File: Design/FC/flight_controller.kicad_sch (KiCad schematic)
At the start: 44 parts, among them U1 STM32H747BIT6, U3 BMI323, U4 MMC5983MA, U5 BMP390

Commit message: before shrinking pcb
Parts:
- removed R64: 0, symbol Device:R_Small_US
- added NT7, NT8: NT, Lib:NetTie-2_SMD_Track0.35mm, symbol Device:NetTie_2
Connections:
- net +3.3V: now also NT7.1
- net BARO_INT_1: now also U1.34 (PF10); no longer U1.26 (PF4)
- net BARO_SPI_NSS: now also U1.30 (PF6); no longer U1.25 (PF3)
- net GND: now also NT8.2; no longer U1.194 (BOOT0)
- net MAG_SPI_NSS: now also U1.26 (PF4); no longer U1.34 (PF10)
- net NRST: now also NT7.2
- net R_SERVO_2_SIGNAL: no longer U1.205 (PI6)
- net EXT_6_DEV_INT_MAG renamed EXT_3_DEV_INT
- net EXT_3_DEV_INT: now also U1.25 (PF3); no longer U1.30 (PF6)
- new net BOOT0: NT8.1, U1.194 (BOOT0)
- no-connect marks 106 -> 107
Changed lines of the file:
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@@
 	)
 	(no_connect
+		(at 57.15 392.43)
+	)
+	(no_connect
 		(at 55.88 248.92)
 	)
@@
 	(wire
 		(pts
-			(xy 52.07 392.43) (xy 57.15 392.43)
-		)
-		(stroke
-			(width 0)
-			(type default)
-		)
-	)
-	(wire
-		(pts
 			(xy 91.44 82.55) (xy 100.33 82.55)
 		)
@@
 	(wire
 		(pts
-			(xy 102.87 382.27) (xy 110.49 382.27)
+			(xy 102.87 382.27) (xy 114.3 382.27)
 		)
 		(stroke
@@
 		)
 	)
+	(label "BOOT0"
+		(at 104.14 382.27 0)
+		(effects
+			(font
+				(size 1.27 1.27)
+			)
+			(justify left bottom)
+		)
+	)
 	(global_label "LED_FC_4"
 		(shape input)
@@
 		)
 	)
-	(global_label "EXT_3_DEV_INT_BARO"
+	(global_label "EXT_10_DEV_INT"
 		(shape input)
-		(at 55.88 297.18 180)
+		(at 55.88 314.96 180)
 		(fields_autoplaced yes)
 		(effects
@@
 		)
 		(property "Intersheetrefs" "${INTERSHEET_REFS}"
-			(at 33.1192 297.18 0)
+			(at 37.8364 314.96 0)
 			(effects
 				(font
@@
 		)
 	)
-	(global_label "SPI_5_NSS_MAG"
+	(global_label "SPI_5_NSS_1"
 		(shape input)
 		(at 91.44 60.96 180)
@@
 		)
 		(property "Intersheetrefs" "${INTERSHEET_REFS}"
-			(at 73.6987 60.96 0)
+			(at 76.2992 60.96 0)
 			(effects
 				(font
@@
 		)
 	)
-	(global_label "EXT_6_DEV_INT_MAG"
+	(global_label "EXT_3_DEV_INT"
 		(shape input)
 		(at 91.44 63.5 180)
@@
 		)
 		(property "Intersheetrefs" "${INTERSHEET_REFS}"
-			(at 69.8283 63.5 0)
+			(at 74.6059 63.5 0)
 			(effects
 				(font
@@
 		)
 	)
-	(global_label "EXT_6_DEV_INT_MAG"
+	(global_label "EXT_3_DEV_INT"
 		(shape input)
-		(at 55.88 304.8 180)
+		(at 55.88 297.18 180)
 		(fields_autoplaced yes)
 		(effects
@@
 		)
 		(property "Intersheetrefs" "${INTERSHEET_REFS}"
-			(at 34.2683 304.8 0)
+			(at 39.0459 297.18 0)
 			(effects
 				(font
@@
 		)
 	)
-	(global_label "EXT_3_DEV_INT_BARO"
+	(global_label "EXT_10_DEV_INT"
 		(shape input)
-		(at 91.44 80.01 180)
+		(at 91.44 82.55 180)
 		(fields_autoplaced yes)
 		(effects
@@
 		)
 		(property "Intersheetrefs" "${INTERSHEET_REFS}"
-			(at 68.6792 80.01 0)
+			(at 73.3964 82.55 0)
 			(effects
 				(font
@@
 		)
 	)
-	(global_label "SPI_5_NSS_MAG"
+	(global_label "SPI_5_NSS_1"
 		(shape input)
-		(at 55.88 314.96 180)
+		(at 55.88 299.72 180)
 		(fields_autoplaced yes)
 		(effects
@@
 		)
 		(property "Intersheetrefs" "${INTERSHEET_REFS}"
-			(at 38.1387 314.96 0)
+			(at 40.7392 299.72 0)
 			(effects
 				(font
@@
 		)
 	)
-	(global_label "TIM_8_CH_2"
-		(shape input)
-		(at 52.07 392.43 180)
-		(fields_autoplaced yes)
-		(effects
-			(font
-				(size 1.27 1.27)
-			)
-			(justify right)
-		)
-		(property "Intersheetrefs" "${INTERSHEET_REFS}"
-			(at 38.1387 392.43 0)
-			(effects
-				(font
-					(size 1.27 1.27)
-				)
-				(justify right)
-				(hide yes)
-			)
-		)
-	)
 	(global_label "BARO_SPI_MISO"
 		(shape input)
@@
 		)
 	)
-	(global_label "SPI_5_NSS_BARO"
+	(global_label "SPI_5_NSS_2"
 		(shape input)
-		(at 91.44 82.55 180)
+		(at 91.44 80.01 180)
 		(fields_autoplaced yes)
 		(effects
@@
 		)
 		(property "Intersheetrefs" "${INTERSHEET_REFS}"
-			(at 72.5496 82.55 0)
+			(at 76.2992 80.01 0)
 			(effects
 				(font
@@
 		)
 	)
-	(global_label "SPI_5_NSS_BARO"
+	(global_label "SPI_5_NSS_2"
 		(shape input)
-		(at 55.88 299.72 180)
+		(at 55.88 304.8 180)
 		(fields_autoplaced yes)
 		(effects
@@
 		)
 		(property "Intersheetrefs" "${INTERSHEET_REFS}"
-			(at 36.9896 299.72 0)
+			(at 40.7392 304.8 0)
 			(effects
 				(font
@@
 	)
 	(symbol
+		(lib_id "Device:NetTie_2")
+		(at 116.84 382.27 0)
+		(unit 1)
+		(exclude_from_sim no)
+		(in_bom no)
+		(on_board yes)
+		(dnp no)
+		(property "Reference" "NT8"
+			(at 116.84 381 0)
+			(effects
+				(font
+					(size 1.27 1.27)
+				)
+			)
+		)
+		(property "Value" "NT"
+			(at 117.094 383.54 0)
+			(effects
+				(font
+					(size 1.27 1.27)
+				)
+			)
+		)
+		(property "Footprint" "Lib:NetTie-2_SMD_Track0.35mm"
+			(at 116.84 382.27 0)
+			(effects
+				(font
+					(size 1.27 1.27)
+				)
+				(hide yes)
+			)
+		)
+		(property "Datasheet" "~"
+			(at 116.84 382.27 0)
+			(effects
+				(font
+					(size 1.27 1.27)
+				)
+				(hide yes)
+			)
+		)
+		(property "Description" "Net tie, 2 pins"
+			(at 116.84 382.27 0)
+			(effects
+				(font
+					(size 1.27 1.27)
+				)
+				(hide yes)
+			)
+		)
+		(pin "1"
+		)
+		(pin "2"
+		)
+		(instances
+			(project "fc"
+				(path "/b150e79a-000e-446c-9119-0865a2de86ff/ef3444a3-41e3-41ea-8a4e-a671b048941e"
+					(reference "NT8")
+					(unit 1)
+				)
+			)
+		)
+	)
+	(symbol
 		(lib_id "Connector_Generic:Conn_01x03")
 		(at 195.58 184.15 90)
@@
 	(symbol
 		(lib_id "power:GND")
-		(at 110.49 382.27 0)
+		(at 119.38 382.27 0)
 		(unit 1)
 		(exclude_from_sim no)
@@
 		(dnp no)
 		(property "Reference" "#PWR086"
-			(at 110.49 388.62 0)
+			(at 119.38 388.62 0)
 			(effects
 				(font
@@
 		)
 		(property "Value" "GND"
-			(at 110.49 386.334 0)
+			(at 119.38 386.334 0)
 			(effects
 				(font
@@
 		)
 		(property "Footprint" ""
-			(at 110.49 382.27 0)
+			(at 119.38 382.27 0)
 			(effects
 				(font
@@
 		)
 		(property "Datasheet" ""
-			(at 110.49 382.27 0)
+			(at 119.38 382.27 0)
 			(effects
 				(font
@@
 		)
 		(property "Description" "Power symbol creates a global label with name \"GND\" , ground"
-			(at 110.49 382.27 0)
+			(at 119.38 382.27 0)
 			(effects
 				(font
@@
 	)
 	(symbol
+		(lib_id "Device:NetTie_2")
+		(at 180.34 52.07 270)
+		(unit 1)
+		(exclude_from_sim no)
+		(in_bom no)
+		(on_board yes)
+		(dnp no)
+		(fields_autoplaced yes)
+		(property "Reference" "NT7"
+			(at 181.61 50.7999 90)
+			(effects
+				(font
+					(size 1.27 1.27)
+				)
+				(justify left)
+			)
+		)
+		(property "Value" "NT"
+			(at 181.61 53.3399 90)
+			(effects
+				(font
+					(size 1.27 1.27)
+				)
+				(justify left)
+			)
+		)
+		(property "Footprint" "Lib:NetTie-2_SMD_Track0.35mm"
+			(at 180.34 52.07 0)
+			(effects
+				(font
+					(size 1.27 1.27)
+				)
+				(hide yes)
+			)
+		)
+		(property "Datasheet" "~"
+			(at 180.34 52.07 0)
+			(effects
+				(font
+					(size 1.27 1.27)
+				)
+				(hide yes)
+			)
+		)
+		(property "Description" "Net tie, 2 pins"
+			(at 180.34 52.07 0)
+			(effects
+				(font
+					(size 1.27 1.27)
+				)
+				(hide yes)
+			)
+		)
+		(pin "1"
+		)
+		(pin "2"
+		)
+		(instances
+			(project "fc"
+				(path "/b150e79a-000e-446c-9119-0865a2de86ff/ef3444a3-41e3-41ea-8a4e-a671b048941e"
+					(reference "NT7")
+					(unit 1)
+				)
+			)
+		)
+	)
+	(symbol
 		(lib_id "power:+5V")
 		(at 193.04 223.52 0)
@@
 					(unit 1)
 				)
-			)
-		)
-	)
-	(symbol
-		(lib_id "Device:R_Small_US")
-		(at 180.34 52.07 180)
-		(unit 1)
-		(exclude_from_sim no)
-		(in_bom no)
-		(on_board no)
-		(dnp no)
-		(property "Reference" "R64"
-			(at 179.324 53.34 0)
-			(effects
-				(font
-					(size 1.27 1.27)
-				)
-				(justify left)
-				(hide yes)
-			)
-		)
-		(property "Value" "0"
-			(at 179.324 51.816 0)
-			(effects
-				(font
-					(size 1.27 1.27)
-				)
-				(justify left)
-			)
-		)
-		(property "Footprint" ""
-			(at 180.34 52.07 0)
-			(effects
-				(font
-					(size 1.27 1.27)
-				)
-				(hide yes)
-			)
-		)
-		(property "Datasheet" "~"
-			(at 180.34 52.07 0)
-			(effects
-				(font
-					(size 1.27 1.27)
-				)
-				(hide yes)
-			)
-		)
-		(property "Description" "Resistor, small US symbol"
-			(at 180.34 52.07 0)
-			(effects
-				(font
-					(size 1.27 1.27)
-				)
-				(hide yes)
-			)
-		)
-		(pin "1"
-		)
-		(pin "2"
-		)
-		(instances
-			(project "fc"
-				(path "/b150e79a-000e-446c-9119-0865a2de86ff/ef3444a3-41e3-41ea-8a4e-a671b048941e"
-					(reference "R64")
-					(unit 1)
-				)

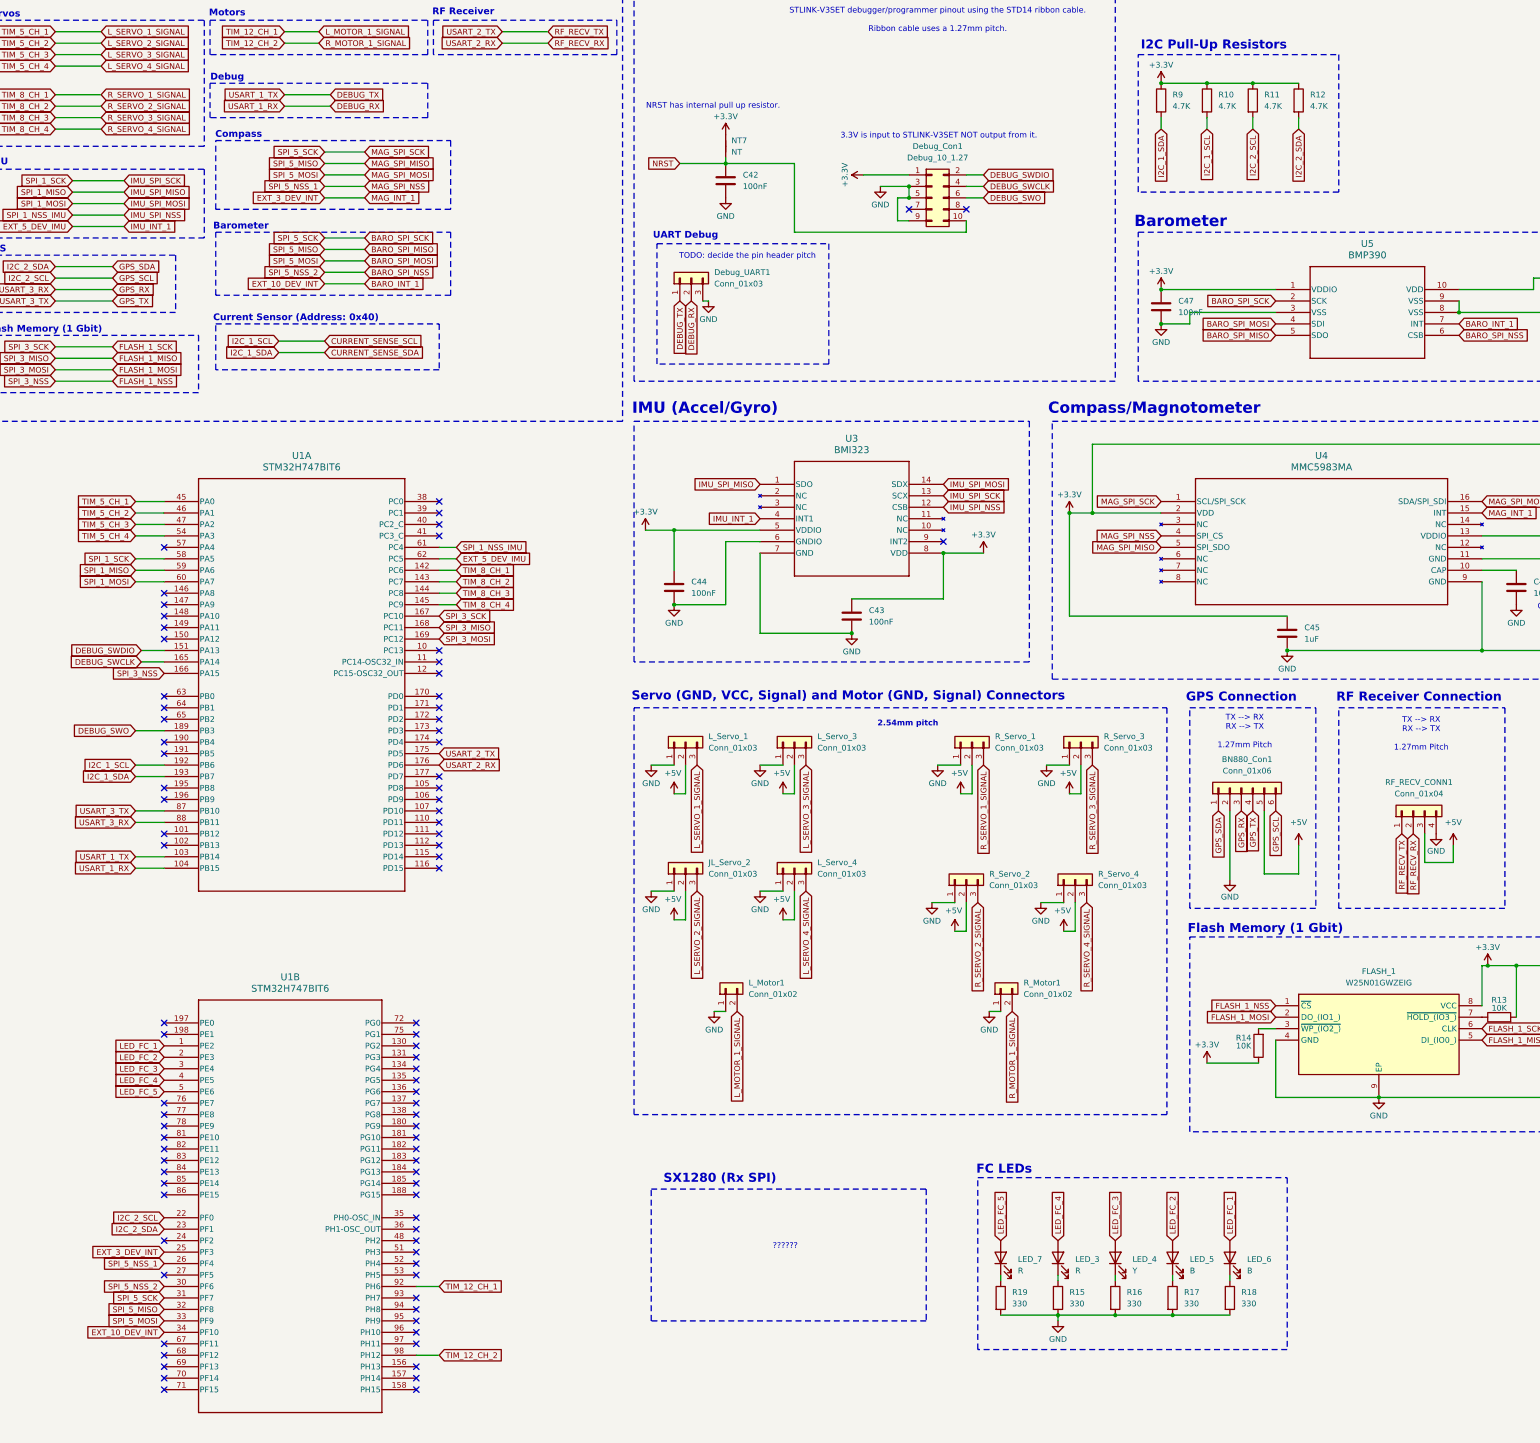
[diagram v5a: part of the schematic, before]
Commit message: finished pcb layout and started on bom
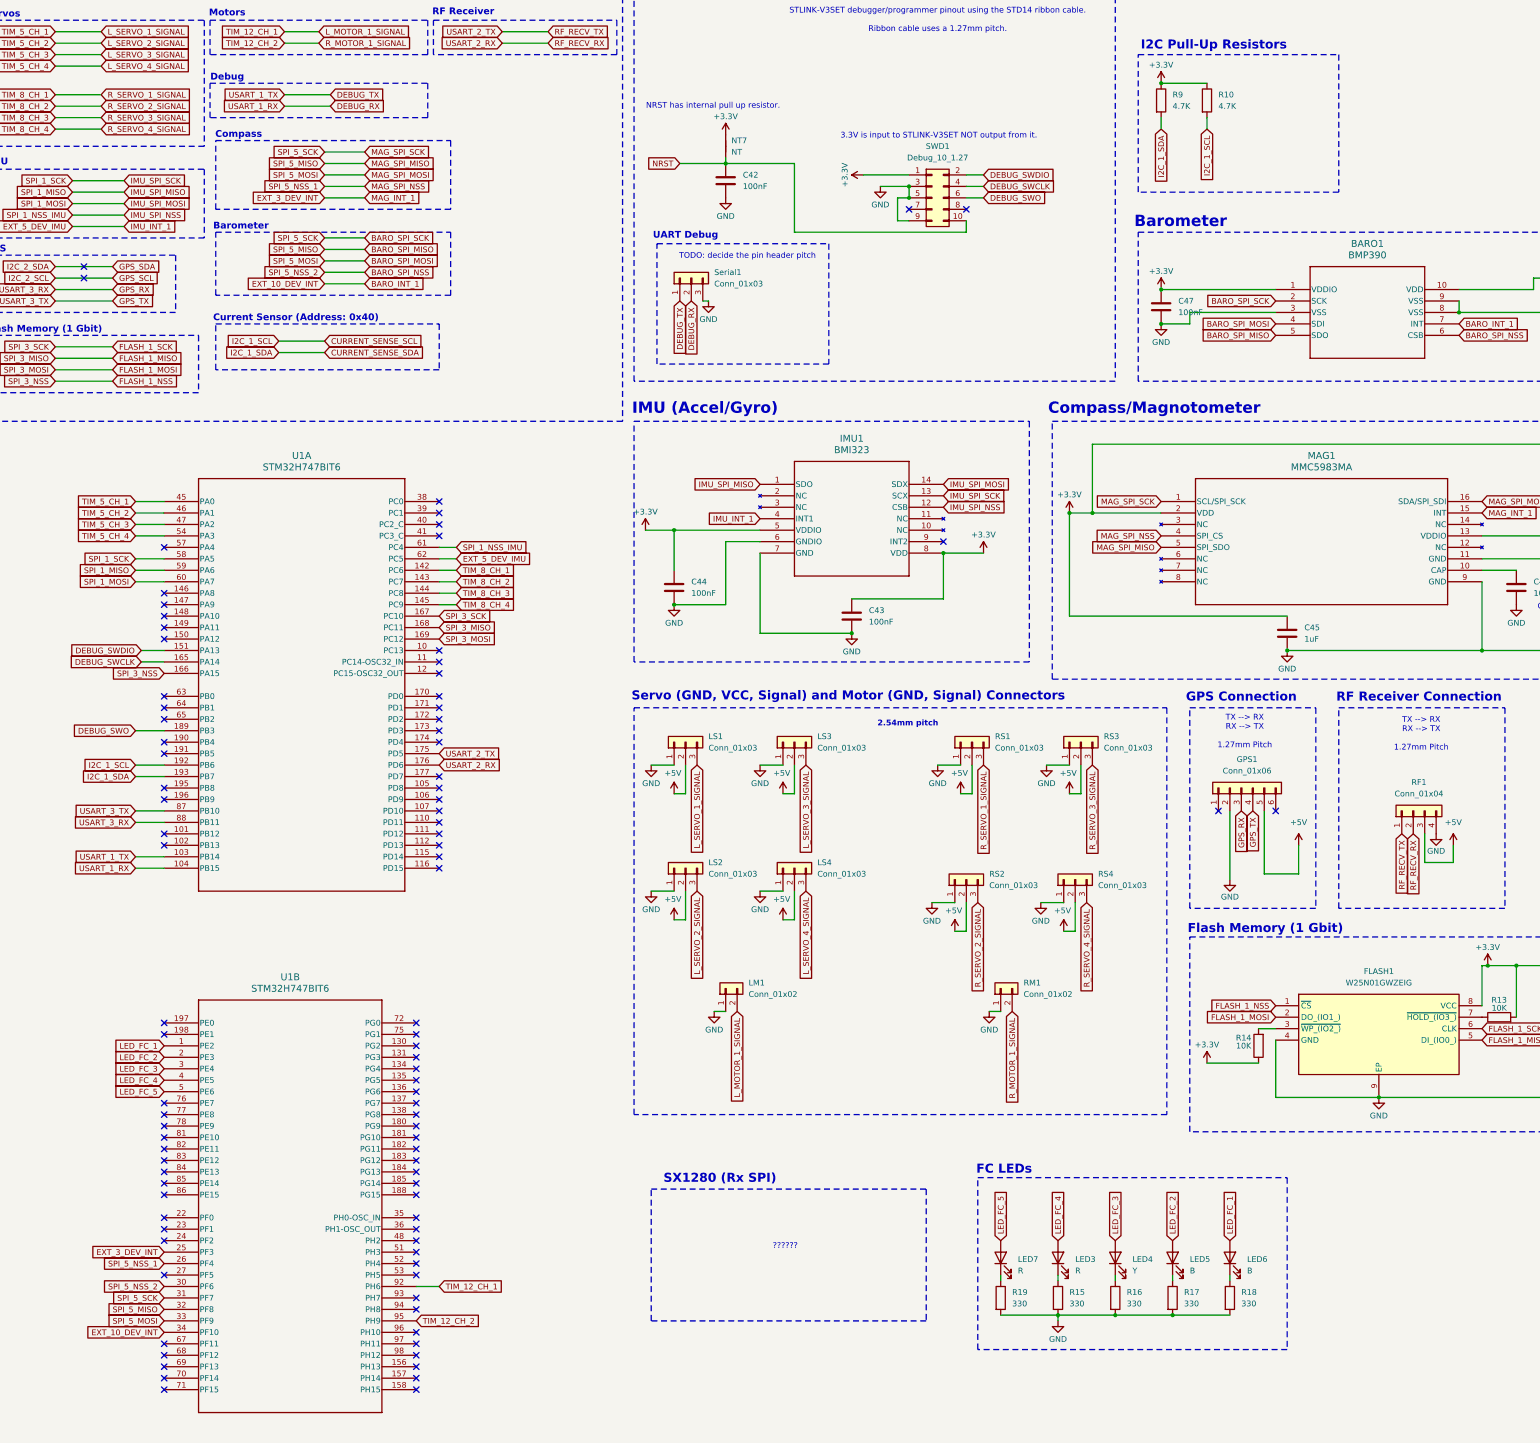
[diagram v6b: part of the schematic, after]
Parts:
- removed R11, R12: 4.7K, Resistor_SMD:R_0603_1608Metric_Pad0.98x0.95mm_HandSolder, symbol Device:R
- BARO1: renamed from U5; Manufacturer_Name (none) -> Bosch Sensortec; Manufacturer_Part_Number (none) -> BMP390; PACKAGE_TYPE (none) -> SMD 10LGA
- C42, C43, C44, C47, C48, C49: Manufacturer_Name (none) -> YAGEO; Manufacturer_Part_Number (none) -> CC0603KRX7R7BB104; PACKAGE_TYPE (none) -> SMD 0603
- C45: Manufacturer_Name (none) -> Samsung Electro-Mechanics; Manufacturer_Part_Number (none) -> CL10B105KO8NNNC; PACKAGE_TYPE (none) -> SMD 0603
- C46: footprint Capacitor_SMD:C_0603_1608Metric_Pad1.08x0.95mm_HandSolder -> Capacitor_SMD:C_0805_2012Metric_Pad1.18x1.45mm_HandSolder; Manufacturer_Name (none) -> KEMET; Manufacturer_Part_Number (none) -> C0805C106K8RACTU; PACKAGE_TYPE (none) -> SMD 0805
- FLASH1: renamed from FLASH_1; PACKAGE_TYPE (none) -> 8WSON
- GPS1: renamed from BN880_Con1; footprint Connector_PinHeader_1.27mm:PinHeader_1x06_P1.27mm_Horizontal -> Molex:CONN_532610001-SD_06Pin_1.25mm; Manufacturer_Name (none) -> Molex; Manufacturer_Part_Number (none) -> 0532610671; PACKAGE_TYPE (none) -> SMD R/A 6POS
- IMU1: renamed from U3; Manufacturer_Name (none) -> Bosch Sensortec; Manufacturer_Part_Number (none) -> BMI323; PACKAGE_TYPE (none) -> 14LGA
- LED3: renamed from LED_3; Manufacturer_Name (none) -> Lite-On Inc.; Manufacturer_Part_Number (none) -> LTST-C191KRKT; PACKAGE_TYPE (none) -> SMD 0603
- LED4: renamed from LED_4; Manufacturer_Name (none) -> Lite-On Inc.; Manufacturer_Part_Number (none) -> LTST-C191KSKT; PACKAGE_TYPE (none) -> SMD 0603
- LED7: renamed from LED_7; Manufacturer_Name (none) -> Lite-On Inc.; Manufacturer_Part_Number (none) -> LTST-C191KRKT; PACKAGE_TYPE (none) -> SMD 0603
- RF1: renamed from RF_RECV_CONN1; footprint Connector_PinHeader_1.27mm:PinHeader_1x04_P1.27mm_Horizontal -> Molex:CONN_532610471_SMD_4Pin_1.25mm
- SWD1: renamed from Debug_Con1; footprint Connector_PinHeader_1.27mm:PinHeader_2x05_P1.27mm_Vertical -> Connectors:CONN_GRPB052VWQS-RC_OddEven_2x5Pins_1.27mm
- renumbered LED_5 to LED5, LED_6 to LED6, L_Motor1 to LM1, L_Servo_1 to LS1, JL_Servo_2 to LS2, L_Servo_3 to LS3, L_Servo_4 to LS4, U4 to MAG1, R_Motor1 to RM1, R_Servo_1 to RS1, R_Servo_2 to RS2, R_Servo_3 to RS3, R_Servo_4 to RS4, Debug_UART1 to Serial1
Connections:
- net GPS_SCL: no longer GPS1.6 (Pin_6), U1.22 (PF0)
- net GPS_SDA: no longer GPS1.1 (Pin_1), U1.23 (PF1)
- net R_MOTOR_1_SIGNAL: now also U1.95 (PH9); no longer U1.98 (PH12)
- no-connect marks 107 -> 113

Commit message: finished filling out bom
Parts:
- LED5, LED6: Manufacturer_Name (none) -> Lite-On Inc.; Manufacturer_Part_Number (none) -> LTST-C193TBKT-5A; PACKAGE_TYPE (none) -> SMD 0603
- LM1, RM1: Manufacturer_Name (none) -> JST Sales America Inc.; Manufacturer_Part_Number (none) -> B2B-XH-A; PACKAGE_TYPE (none) -> TH 2.5mm
- LS1, LS2, LS3, LS4, RS1, RS2, RS3, RS4, Serial1: Manufacturer_Name (none) -> JST Sales America Inc.; Manufacturer_Part_Number (none) -> B3B-XH-A; PACKAGE_TYPE (none) -> TH 2.5mm
- MAG1: Manufacturer_Name (none) -> Memsic Inc.; Manufacturer_Part_Number (none) -> MMC5983MA; PACKAGE_TYPE (none) -> 16-LGA (3x3)
- R10, R9: Manufacturer_Name (none) -> TE Connectivity Passive Product; Manufacturer_Part_Number (none) -> CRGP0603F4K7; PACKAGE_TYPE (none) -> SMD 0603
- R13, R14: Manufacturer_Name (none) -> TE Connectivity Passive Product; Manufacturer_Part_Number (none) -> CRGP0603F10K; PACKAGE_TYPE (none) -> SMD 0603
- R15, R16, R17, R18, R19: Manufacturer_Name (none) -> TE Connectivity Passive Product; Manufacturer_Part_Number (none) -> CRGP0603F330R; PACKAGE_TYPE (none) -> SMD 0603
- SWD1: Manufacturer_Name (none) -> Sullins Connector Solutions; Manufacturer_Part_Number (none) -> GRPB052VWQS-RC; PACKAGE_TYPE (none) -> 2x5 1.27mm Right Angle SMD
- U1: Manufacturer_Name (none) -> STMicroelectronics; Manufacturer_Part_Number (none) -> STM32H747BIT6; PACKAGE_TYPE (none) -> 208LQFP
